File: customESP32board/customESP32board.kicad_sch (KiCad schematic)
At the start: 50 parts, among them J1 USB_B, J2 Conn_01x16_Pin, J3 Conn_01x16_Pin, Q1 S8050, Q2 S8050, Q3 BSS138, Q4 BSS138, Q5 BSS138, SW1 SW_Push, SW2 SW_Push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

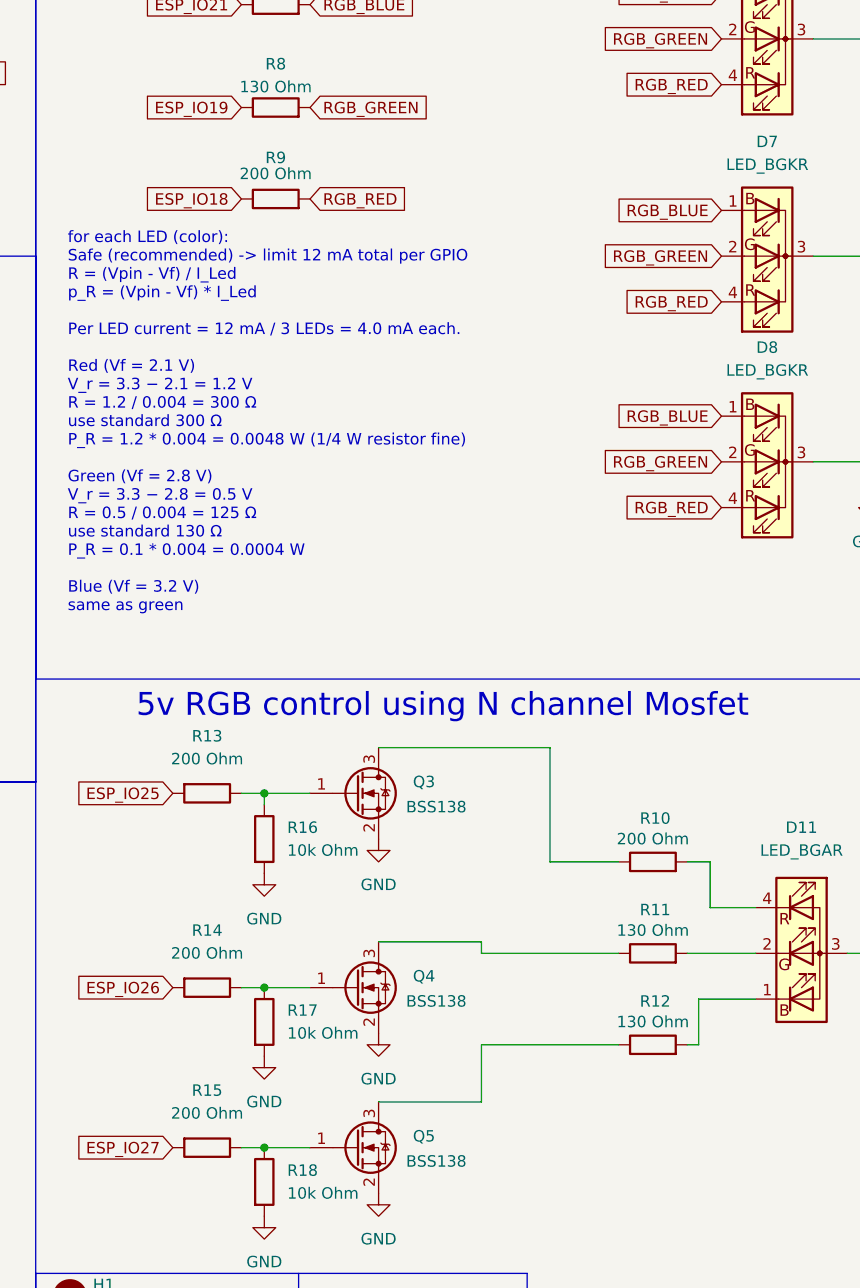
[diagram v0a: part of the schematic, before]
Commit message: updated schematic -> components foot print and BOM
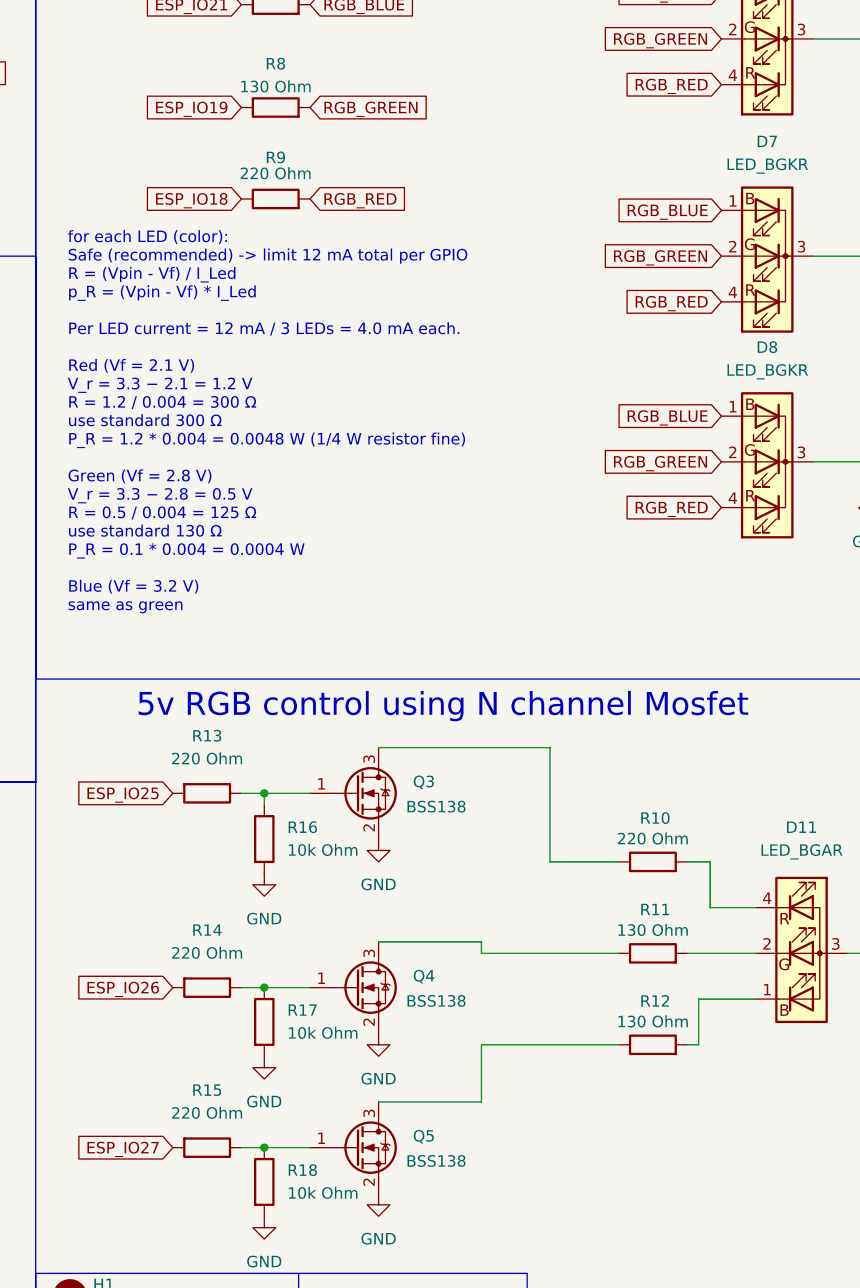
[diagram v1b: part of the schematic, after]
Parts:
- C1, C7: link https://makerselectronics.com/product/multilayer-ceramic-capacitors-mlcc-smd-smt-10uf-%c2%b110-25v-0805/ -> https://makerselectronics.com/product/multilayer-ceramic-capacitors-mlcc-smd-smt-10uf-50v-x5r-%c2%b110-1206/
- C3, C6: link https://makerselectronics.com/product/multilayer-ceramic-sm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 -> https://makerselectronics.com/product/multilayer-ceramic-ca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
- D5: link https://makerselectronics.com/product/smd-led-0603/?srsltid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 -> https://makerselectronics.com/product/smd-led-blue-1206/
- D9: link https://makerselectronics.com/product/smd-led-0603/?srsltid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 -> https://makerselectronics.com/product/smd-led-red-1206/
- R1: link https://makerselectronics.com/product/chip-resistor-smd-2-2k%cf%89-%c2%b15-0-125w-%c2%b1100ppm-c-0805/ -> https://makerselectronics.com/product/chip-resistor-smd-2-2k%cf%89-%c2%b15-250mw-1206/
- R10, R13, R14, R15, R9: value 200 Ohm -> 220 Ohm; link https://uge-one.com/product/smd-chip-resistor-size-0603-220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 -> https://uge-one.com/product/smd-chip-resistor-size-1206-220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
- R16, R17, R18, R2, R3: link https://makerselectronics.com/product/chip-resistor-smd-10k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 -> https://makerselectronics.com/product/chip-resistor-smd-10%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
- R4: link https://makerselectronics.com/product/chip-resistor-smd-1k%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 -> https://makerselectronics.com/product/chip-resistor-smd-9-1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
- R7, R8: link https://uge-one.com/product/smd-chip-resistor-size-0603-220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 -> https://makerselectronics.com/product/chip-resistor-smd-130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
- SW1, SW2: link https://uge-one.com/product/smd-micro-switch-white-tact-s-3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 -> https://uge-one.com/product/smd-micro-push-button-switch-2p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
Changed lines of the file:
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@@
 			)
 		)
-		(property "Value" "200 Ohm"
+		(property "Value" "220 Ohm"
 			(at 140.97 118.11 90)
 			(effects
@@
 			)
 		)
-		(property "link" "https://uge-one.com/product/smd-chip-resistor-size-0603-220r-220-ohm/?srsltid=AfmBOoomwG_Geoc_FRjnR47Tr9Sv5QvKfEbhZOUQ078dQ9qG_okaj9jM"
+		(property "link" "https://uge-one.com/product/smd-chip-resistor-size-1206-220r-ohm/?srsltid=AfmBOoqmkuXwKrfJ3VxJ5AIPn5xc8j2ZOYO0PqRCmSUCAxMBlBADOpRb"
 			(at 140.97 121.92 90)
 			(effects
@@
 			)
 		)
-		(property "Value" "200 Ohm"
+		(property "Value" "220 Ohm"
 			(at 148.59 53.086 90)
 			(effects
@@
 			)
 		)
-		(property "link" "https://uge-one.com/product/smd-chip-resistor-size-0603-220r-220-ohm/?srsltid=AfmBOoomwG_Geoc_FRjnR47Tr9Sv5QvKfEbhZOUQ078dQ9qG_okaj9jM"
+		(property "link" "https://uge-one.com/product/smd-chip-resistor-size-1206-220r-ohm/?srsltid=AfmBOoqmkuXwKrfJ3VxJ5AIPn5xc8j2ZOYO0PqRCmSUCAxMBlBADOpRb"
 			(at 148.59 55.88 90)
 			(effects
@@
 			)
 		)
-		(property "link" "https://makerselectronics.com/product/chip-resistor-smd-10k%cf%89-%c2%b11-0-125w-%c2%b1100ppm-%e2%84%83-0805/"
+		(property "link" "https://makerselectronics.com/product/chip-resistor-smd-10%cf%89-%c2%b15-250mw-1206/"
 			(at 147.32 127 0)
 			(effects
@@
 			)
 		)
-		(property "link" "https://makerselectronics.com/product/chip-resistor-smd-10k%cf%89-%c2%b11-0-125w-%c2%b1100ppm-%e2%84%83-0805/"
+		(property "link" "https://makerselectronics.com/product/chip-resistor-smd-10%cf%89-%c2%b15-250mw-1206/"
 			(at 147.32 165.1 0)
 			(effects
@@
 			)
 		)
-		(property "link" "https://makerselectronics.com/product/chip-resistor-smd-10k%cf%89-%c2%b11-0-125w-%c2%b1100ppm-%e2%84%83-0805/"
+		(property "link" "https://makerselectronics.com/product/chip-resistor-smd-10%cf%89-%c2%b15-250mw-1206/"
 			(at 87.63 149.86 90)
 			(effects
@@
 			)
 		)
-		(property "link" "https://uge-one.com/product/smd-micro-switch-white-tact-s-3-6-5-2-pin/"
+		(property "link" "https://uge-one.com/product/smd-micro-push-button-switch-2p-3x4x2mm/"
 			(at 92.71 46.99 90)
 			(effects
@@
 			)
 		)
-		(property "link" "https://makerselectronics.com/product/chip-resistor-smd-10k%cf%89-%c2%b11-0-125w-%c2%b1100ppm-%e2%84%83-0805/"
+		(property "link" "https://makerselectronics.com/product/chip-resistor-smd-10%cf%89-%c2%b15-250mw-1206/"
 			(at 87.63 175.26 90)
 			(effects
@@
 			)
 		)
-		(property "link" "https://makerselectronics.com/product/multilayer-ceramic-capacitors-mlcc-smd-smt-10uf-%c2%b110-25v-0805/"
+		(property "link" "https://makerselectronics.com/product/multilayer-ceramic-capacitors-mlcc-smd-smt-10uf-50v-x5r-%c2%b110-1206/"
 			(at 62.23 30.48 0)
 			(effects
@@
 			)
 		)
-		(property "Value" "200 Ohm"
+		(property "Value" "220 Ohm"
 			(at 190.5 127 90)
 			(effects
@@
 			)
 		)
-		(property "link" "https://uge-one.com/product/smd-chip-resistor-size-0603-220r-220-ohm/?srsltid=AfmBOoomwG_Geoc_FRjnR47Tr9Sv5QvKfEbhZOUQ078dQ9qG_okaj9jM"
+		(property "link" "https://uge-one.com/product/smd-chip-resistor-size-1206-220r-ohm/?srsltid=AfmBOoqmkuXwKrfJ3VxJ5AIPn5xc8j2ZOYO0PqRCmSUCAxMBlBADOpRb"
 			(at 190.5 129.54 90)
 			(effects
@@
 			)
 		)
-		(property "link" "https://makerselectronics.com/product/multilayer-ceramic-smd-capacitor-mlcc-smd-smt-100nf-%c2%b110-50v-x7r-0603/"
+		(property "link" "https://makerselectronics.com/product/multilayer-ceramic-capacitors-mlcc-smd-smt-50v-100nf-x7r-%c2%b110-1206/"
 			(at 31.75 91.44 0)
 			(effects
@@
 			)
 		)
-		(property "link" "https://makerselectronics.com/product/multilayer-ceramic-capacitors-mlcc-smd-smt-10uf-%c2%b110-25v-0805/"
+		(property "link" "https://makerselectronics.com/product/multilayer-ceramic-capacitors-mlcc-smd-smt-10uf-50v-x5r-%c2%b110-1206/"
 			(at 20.32 91.44 0)
 			(effects
@@
 			)
 		)
-		(property "link" "https://uge-one.com/product/smd-chip-resistor-size-0603-220r-220-ohm/?srsltid=AfmBOoomwG_Geoc_FRjnR47Tr9Sv5QvKfEbhZOUQ078dQ9qG_okaj9jM"
+		(property "link" "https://makerselectronics.com/product/chip-resistor-smd-130%cf%89-%c2%b11-0-125w-0805/"
 			(at 148.59 34.29 90)
 			(effects
@@
 			)
 		)
-		(property "Value" "200 Ohm"
+		(property "Value" "220 Ohm"
 			(at 140.97 139.7 90)
 			(effects
@@
 			)
 		)
-		(property "link" "https://uge-one.com/product/smd-chip-resistor-size-0603-220r-220-ohm/?srsltid=AfmBOoomwG_Geoc_FRjnR47Tr9Sv5QvKfEbhZOUQ078dQ9qG_okaj9jM"
+		(property "link" "https://uge-one.com/product/smd-chip-resistor-size-1206-220r-ohm/?srsltid=AfmBOoqmkuXwKrfJ3VxJ5AIPn5xc8j2ZOYO0PqRCmSUCAxMBlBADOpRb"
 			(at 140.97 143.51 90)
 			(effects
@@
 			)
 		)
-		(property "link" "https://uge-one.com/product/smd-micro-switch-white-tact-s-3-6-5-2-pin/"
+		(property "link" "https://uge-one.com/product/smd-micro-push-button-switch-2p-3x4x2mm/"
 			(at 106.68 46.99 90)
 			(effects
@@
 			)
 		)
-		(property "link" "https://makerselectronics.com/product/multilayer-ceramic-smd-capacitor-mlcc-smd-smt-100nf-%c2%b110-50v-x7r-0603/"
+		(property "link" "https://makerselectronics.com/product/multilayer-ceramic-capacitors-mlcc-smd-smt-50v-100nf-x7r-%c2%b110-1206/"
 			(at 105.41 185.42 90)
 			(effects
@@
 			)
 		)
-		(property "link" "https://makerselectronics.com/product/chip-resistor-smd-2-2k%cf%89-%c2%b15-0-125w-%c2%b1100ppm-c-0805/"
+		(property "link" "https://makerselectronics.com/product/chip-resistor-smd-2-2k%cf%89-%c2%b15-250mw-1206/"
 			(at 90.17 81.28 0)
 			(effects
@@
 			)
 		)
-		(property "Value" "200 Ohm"
+		(property "Value" "220 Ohm"
 			(at 140.97 157.48 90)
 			(effects
@@
 			)
 		)
-		(property "link" "https://uge-one.com/product/smd-chip-resistor-size-0603-220r-220-ohm/?srsltid=AfmBOoomwG_Geoc_FRjnR47Tr9Sv5QvKfEbhZOUQ078dQ9qG_okaj9jM"
+		(property "link" "https://uge-one.com/product/smd-chip-resistor-size-1206-220r-ohm/?srsltid=AfmBOoqmkuXwKrfJ3VxJ5AIPn5xc8j2ZOYO0PqRCmSUCAxMBlBADOpRb"
 			(at 140.97 161.29 90)
 			(effects
@@
 			)
 		)
-		(property "link" "https://uge-one.com/product/smd-chip-resistor-size-0603-220r-220-ohm/?srsltid=AfmBOoomwG_Geoc_FRjnR47Tr9Sv5QvKfEbhZOUQ078dQ9qG_okaj9jM"
+		(property "link" "https://makerselectronics.com/product/chip-resistor-smd-130%cf%89-%c2%b11-0-125w-0805/"
 			(at 148.59 45.72 90)
 			(effects
@@
 			)
 		)
-		(property "link" "https://makerselectronics.com/product/smd-led-0603/?srsltid=AfmBOorYjfgpYXuaPCjOsgniHguapARLiV4EjBLcVDZNF8KNPmgZIGWx"
+		(property "link" "https://makerselectronics.com/product/smd-led-red-1206/"
 			(at 90.17 88.9 0)
 			(effects
@@
 			)
 		)
-		(property "link" "https://makerselectronics.com/product/chip-resistor-smd-10k%cf%89-%c2%b11-0-125w-%c2%b1100ppm-%e2%84%83-0805/"
+		(property "link" "https://makerselectronics.com/product/chip-resistor-smd-10%cf%89-%c2%b15-250mw-1206/"
 			(at 147.32 147.32 0)
 			(effects
@@
 			)
 		)
-		(property "link" "https://makerselectronics.com/product/chip-resistor-smd-1k%cf%89-%c2%b15-0-125w-%c2%b1100ppm-%e2%84%83-0603/"
+		(property "link" "https://makerselectronics.com/product/chip-resistor-smd-9-1k%cf%89-%c2%b15-250mw-1206/"
 			(at 107.95 83.82 0)
 			(effects
@@
 			)
 		)
-		(property "link" "https://makerselectronics.com/product/smd-led-0603/?srsltid=AfmBOorYjfgpYXuaPCjOsgniHguapARLiV4EjBLcVDZNF8KNPmgZIGWx"
+		(property "link" "https://makerselectronics.com/product/smd-led-blue-1206/"
 			(at 107.95 91.44 90)
 			(effects
